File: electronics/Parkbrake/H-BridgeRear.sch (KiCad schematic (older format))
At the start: 82 parts

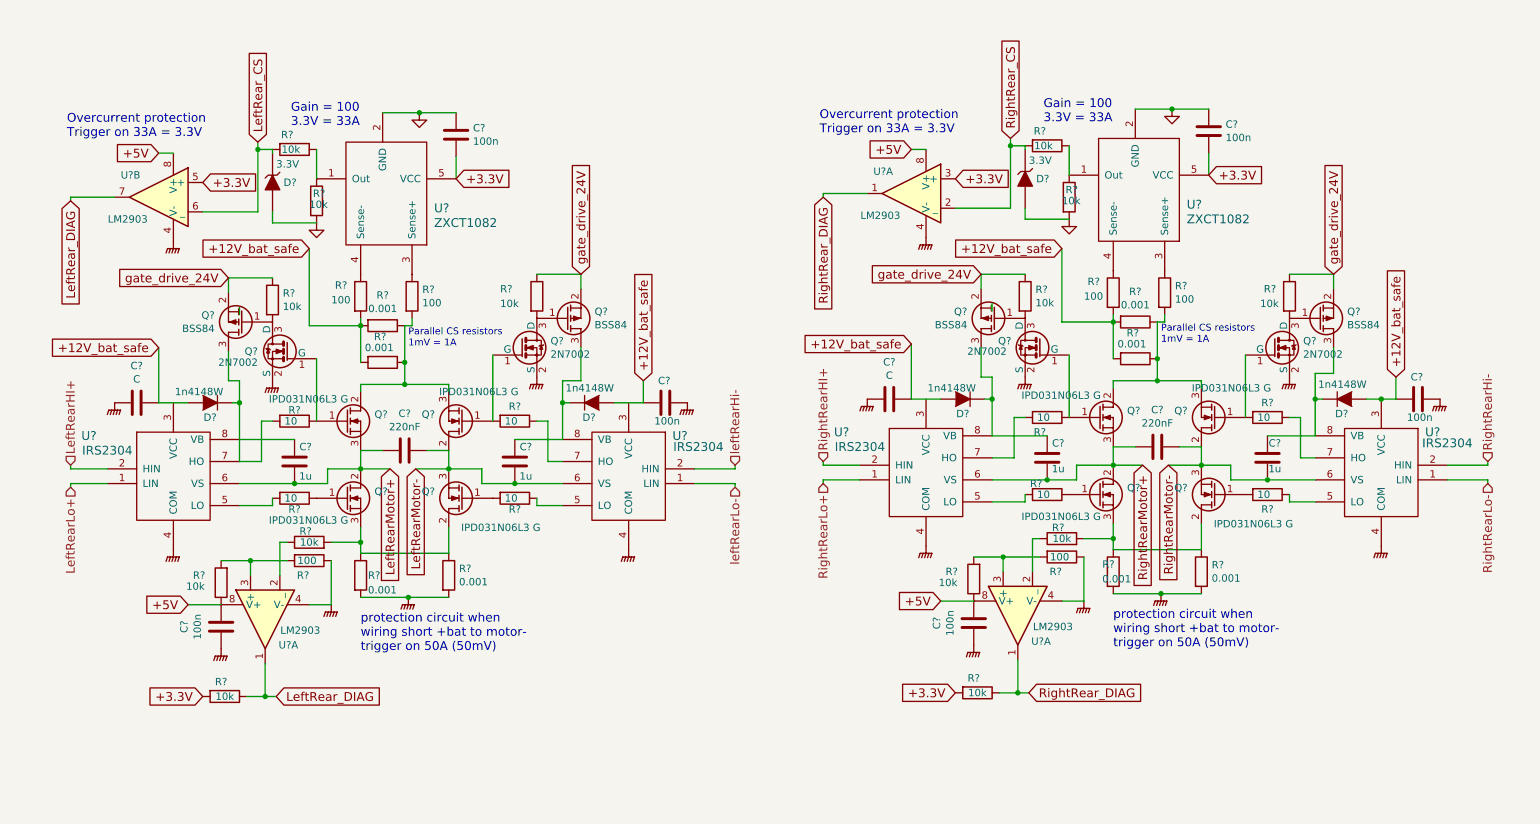
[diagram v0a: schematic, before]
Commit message: Fixes to Bat switch and polarity protection
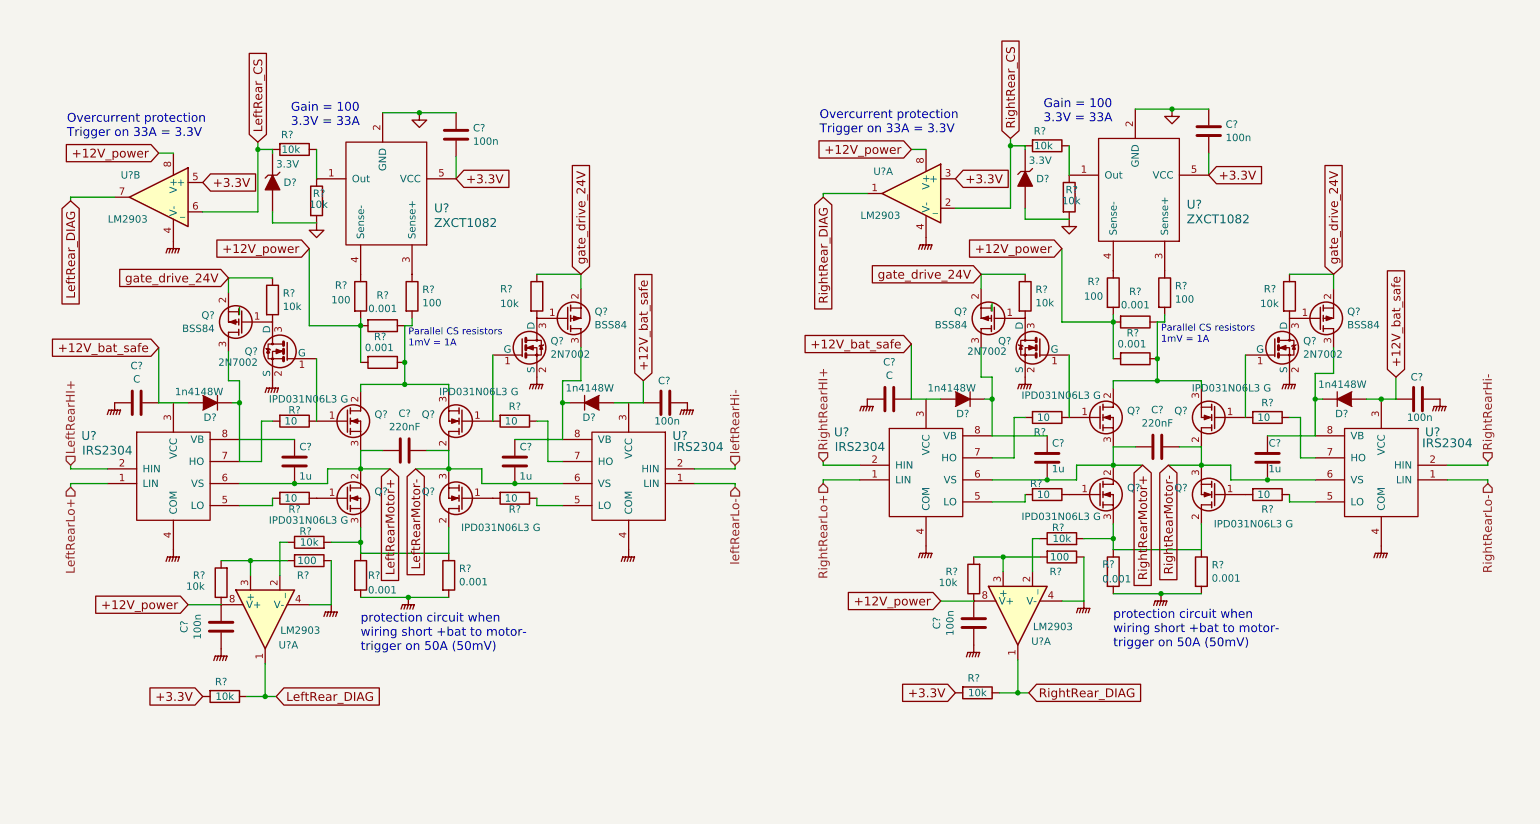
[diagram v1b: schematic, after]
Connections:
- net +12V_bat_safe: no longer R?.2, R?.2, R?.2, R?.2, R?.2, R?.2
- net +5V renamed +12V_power
- net +12V_power: now also R?.2, R?.2, R?.2, R?.2, R?.2, R?.2
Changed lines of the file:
@@
 $EndComp
 Text GLabel 2500 2475 0    60   Input ~ 0
-+12V_bat_safe
++12V_power
 $Comp
 L C C?
@@
 	2250 1800 2250 1825
 Text GLabel 1475 1825 0    60   Input ~ 0
-+5V
++12V_power
 Wire Wire Line
 	1575 1825 1475 1825
@@
 	875  2125 875  2150
 Text GLabel 1675 4900 0    60   Input ~ 0
-+5V
++12V_power
 Text GLabel 1775 2025 2    60   Input ~ 0
 +3.3V
@@
 $EndComp
 Text GLabel 7625 2475 0    60   Input ~ 0
-+12V_bat_safe
++12V_power
 $Comp
 L C C?
@@
 	7375 1775 7375 1800
 Text GLabel 6600 1800 0    60   Input ~ 0
-+5V
++12V_power
 Wire Wire Line
 	6700 1800 6600 1800
@@
 	6000 2100 6000 2125
 Text GLabel 6800 4875 0    60   Input ~ 0
-+5V
++12V_power
 Text GLabel 6900 2000 2    60   Input ~ 0
 +3.3V

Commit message: Add currentlimit latching to avaoid current limit oscilation Start a mcu schema part
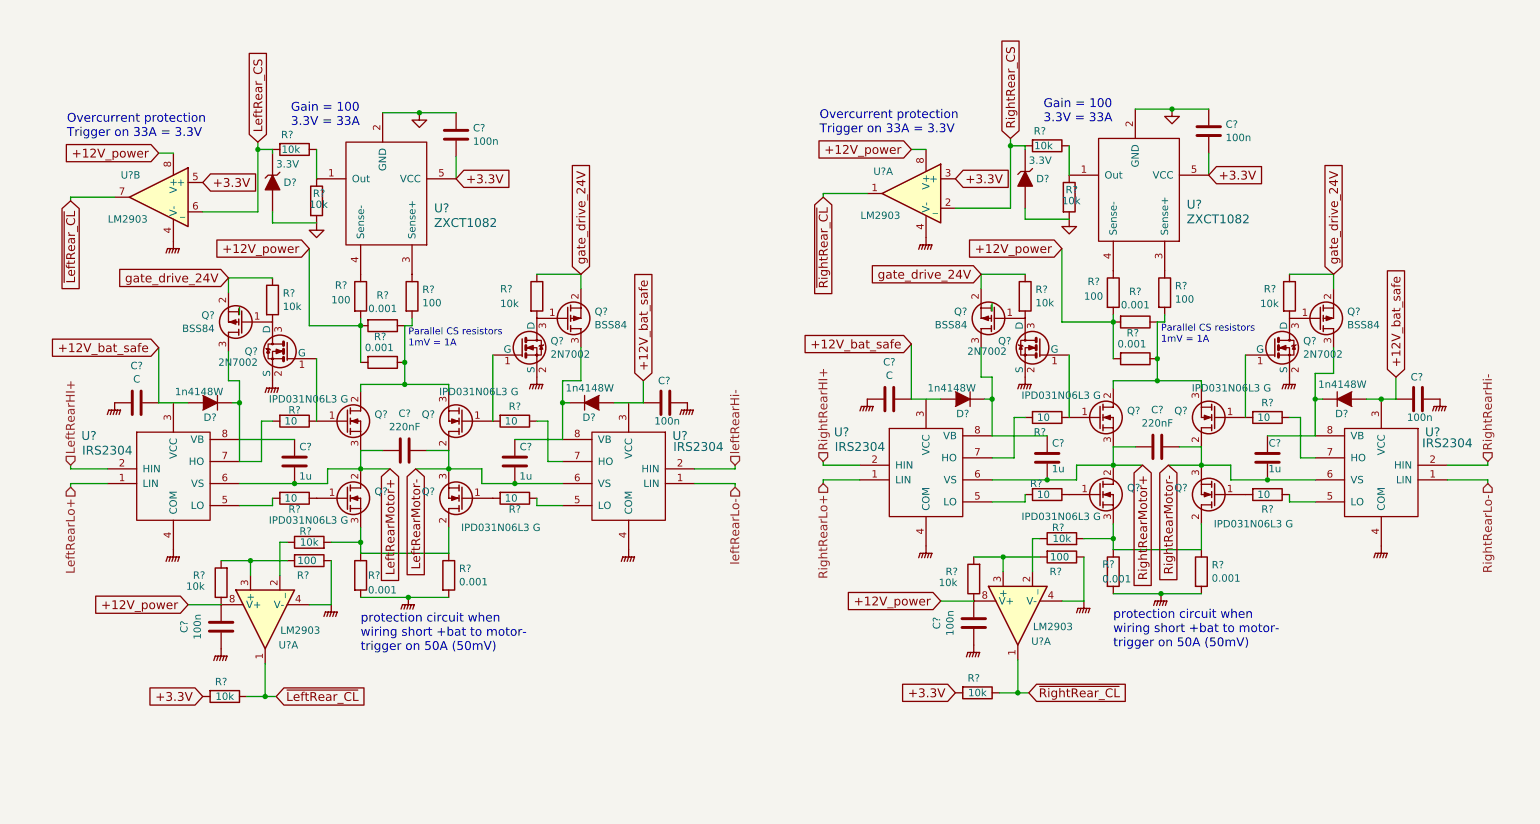
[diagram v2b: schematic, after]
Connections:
- net LeftRear_DIAG renamed ~LeftRear_CL
- net RightRear_DIAG renamed ~RightRear_CL
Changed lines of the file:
@@
 $Descr A4 11693 8268
 encoding utf-8
-Sheet 3 5
+Sheet 3 6
 Title ""
 Date ""
@@
 	4050 4225 4050 4175
 Text GLabel 2275 5525 2    60   Input ~ 0
-LeftRear_DIAG
+~LeftRear_CL
 Text GLabel 3050 3975 3    60   Input ~ 0
 LeftRearMotor+
@@
 LeftRear_CS
 Text GLabel 875  2150 3    60   Input ~ 0
-LeftRear_DIAG
+~LeftRear_CL
 Text GLabel 6000 2125 3    60   Input ~ 0
-RightRear_DIAG
+~RightRear_CL
 Text GLabel 7275 1725 1    60   Input ~ 0
 RightRear_CS
@@
 RightRearMotor-
 Text GLabel 7400 5500 2    60   Input ~ 0
-RightRear_DIAG
+~RightRear_CL
 $EndSCHEMATC

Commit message: More work on parkbrake node
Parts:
- R? (x4): footprint (none) -> Resistors_SMD:R_0805; farnell (none) -> 9332375; part (none) -> MC01W08051100R
- R? (x14): footprint (none) -> Resistors_SMD:R_0805; farnell (none) -> 9332391; part (none) -> MC01W0805110K
- R? (x8): footprint (none) -> Resistors_SMD:R_1206; farnell (none) -> 9335790; part (none) -> MC0125W1206110R
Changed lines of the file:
@@
 LIBS:teensy
 LIBS:power_switches
+LIBS:stm32
 LIBS:Parkbrake-cache
 EELAYER 25 0
@@
 $Descr A4 11693 8268
 encoding utf-8
-Sheet 3 6
+Sheet 3 10
 Title ""
 Date ""
@@
 F 0 "R?" H 3270 2846 50  0000 L CNN
 F 1 "100" H 3270 2755 50  0000 L CNN
-F 2 "" V 3130 2800 50  0000 C CNN
+F 2 "Resistors_SMD:R_0805" V 3130 2800 50  0001 C CNN
 F 3 "" H 3200 2800 50  0000 C CNN
+F 4 "MC01W08051100R" H 3200 2800 60  0001 C CNN "part"
+F 5 "9332375" H 3200 2800 60  0001 C CNN "farnell"
 	1    3200 2800
 	1    0    0    -1
@@
 F 0 "R?" H 2675 2875 50  0000 L CNN
 F 1 "100" H 2650 2775 50  0000 L CNN
-F 2 "" V 2780 2800 50  0000 C CNN
+F 2 "Resistors_SMD:R_0805" V 2780 2800 50  0001 C CNN
 F 3 "" H 2850 2800 50  0000 C CNN
+F 4 "MC01W08051100R" H 2850 2800 60  0001 C CNN "part"
+F 5 "9332375" H 2850 2800 60  0001 C CNN "farnell"
 	1    2850 2800
 	1    0    0    -1
@@
 F 0 "R?" H 2525 2200 50  0000 L CNN
 F 1 "10k" H 2500 2125 50  0000 L CNN
-F 2 "" V 2480 2150 50  0000 C CNN
+F 2 "Resistors_SMD:R_0805" V 2480 2150 50  0001 C CNN
 F 3 "" H 2550 2150 50  0000 C CNN
+F 4 "MC01W0805110K" H 2550 2150 60  0001 C CNN "part"
+F 5 "9332391" H 2550 2150 60  0001 C CNN "farnell"
 	1    2550 2150
 	1    0    0    -1
@@
 F 0 "R?" V 3975 4175 50  0000 C CNN
 F 1 "10" V 3900 4150 50  0000 C CNN
-F 2 "" V 3830 4175 50  0000 C CNN
+F 2 "Resistors_SMD:R_1206" V 3830 4175 50  0001 C CNN
 F 3 "" H 3900 4175 50  0000 C CNN
+F 4 "9335790" V 3900 4175 60  0001 C CNN "farnell"
+F 5 "MC0125W1206110R" V 3900 4175 60  0001 C CNN "part"
 	1    3900 4175
 	0    1    1    0
@@
 F 0 "R?" V 2475 4175 50  0000 C CNN
 F 1 "10" V 2400 4150 50  0000 C CNN
-F 2 "" V 2330 4175 50  0000 C CNN
+F 2 "Resistors_SMD:R_1206" V 2330 4175 50  0001 C CNN
 F 3 "" H 2400 4175 50  0000 C CNN
+F 4 "9335790" V 2400 4175 60  0001 C CNN "farnell"
+F 5 "MC0125W1206110R" V 2400 4175 60  0001 C CNN "part"
 	1    2400 4175
 	0    1    1    0
@@
 F 0 "R?" V 2325 3650 50  0000 C CNN
 F 1 "10" V 2400 3625 50  0000 C CNN
-F 2 "" V 2330 3650 50  0000 C CNN
+F 2 "Resistors_SMD:R_1206" V 2330 3650 50  0001 C CNN
 F 3 "" H 2400 3650 50  0000 C CNN
+F 4 "9335790" V 2400 3650 60  0001 C CNN "farnell"
+F 5 "MC0125W1206110R" V 2400 3650 60  0001 C CNN "part"
 	1    2400 3650
 	0    1    1    0
@@
 F 0 "R?" V 3800 3650 50  0000 C CNN
 F 1 "10" V 3900 3625 50  0000 C CNN
-F 2 "" V 3830 3650 50  0000 C CNN
+F 2 "Resistors_SMD:R_1206" V 3830 3650 50  0001 C CNN
 F 3 "" H 3900 3650 50  0000 C CNN
+F 4 "9335790" V 3900 3650 60  0001 C CNN "farnell"
+F 5 "MC0125W1206110R" V 3900 3650 60  0001 C CNN "part"
 	1    3900 3650
 	0    1    1    0
@@
 F 0 "R?" H 2050 4700 50  0000 C CNN
 F 1 "10k" H 2075 4775 50  0000 C CNN
-F 2 "" V 1830 4750 50  0000 C CNN
+F 2 "Resistors_SMD:R_0805" V 1830 4750 50  0001 C CNN
 F 3 "" H 1900 4750 50  0000 C CNN
+F 4 "MC01W0805110K" H 1900 4750 60  0001 C CNN "part"
+F 5 "9332391" H 1900 4750 60  0001 C CNN "farnell"
 	1    1900 4750
 	-1   0    0    1
@@
 F 0 "R?" V 2575 4500 50  0000 C CNN
 F 1 "10k" V 2500 4475 50  0000 C CNN
-F 2 "" V 2430 4475 50  0000 C CNN
+F 2 "Resistors_SMD:R_0805" V 2430 4475 50  0001 C CNN
 F 3 "" H 2500 4475 50  0000 C CNN
+F 4 "MC01W0805110K" V 2500 4475 60  0001 C CNN "part"
+F 5 "9332391" V 2500 4475 60  0001 C CNN "farnell"
 	1    2500 4475
 	0    -1   -1   0
@@
 F 0 "R?" V 1825 5500 50  0000 C CNN
 F 1 "10k" V 1925 5525 50  0000 C CNN
-F 2 "" V 1855 5525 50  0000 C CNN
+F 2 "Resistors_SMD:R_0805" V 1855 5525 50  0001 C CNN
 F 3 "" H 1925 5525 50  0000 C CNN
+F 4 "MC01W0805110K" V 1925 5525 60  0001 C CNN "part"
+F 5 "9332391" V 1925 5525 60  0001 C CNN "farnell"
 	1    1925 5525
 	0    1    1    0
@@
 F 0 "R?" V 2300 1750 50  0000 C CNN
 F 1 "10k" V 2400 1775 50  0000 C CNN
-F 2 "" V 2330 1800 50  0000 C CNN
+F 2 "Resistors_SMD:R_0805" V 2330 1800 50  0001 C CNN
 F 3 "" H 2400 1800 50  0000 C CNN
+F 4 "MC01W0805110K" V 2400 1800 60  0001 C CNN "part"
+F 5 "9332391" V 2400 1800 60  0001 C CNN "farnell"
 	1    2400 1800
 	0    1    1    0
@@
 F 0 "R?" H 8395 2821 50  0000 L CNN
 F 1 "100" H 8395 2730 50  0000 L CNN
-F 2 "" V 8255 2775 50  0000 C CNN
+F 2 "Resistors_SMD:R_0805" V 8255 2775 50  0001 C CNN
 F 3 "" H 8325 2775 50  0000 C CNN
+F 4 "MC01W08051100R" H 8325 2775 60  0001 C CNN "part"
+F 5 "9332375" H 8325 2775 60  0001 C CNN "farnell"
 	1    8325 2775
 	1    0    0    -1
@@
 F 0 "R?" H 7800 2850 50  0000 L CNN
 F 1 "100" H 7775 2750 50  0000 L CNN
-F 2 "" V 7905 2775 50  0000 C CNN
+F 2 "Resistors_SMD:R_0805" V 7905 2775 50  0001 C CNN
 F 3 "" H 7975 2775 50  0000 C CNN
+F 4 "MC01W08051100R" H 7975 2775 60  0001 C CNN "part"
+F 5 "9332375" H 7975 2775 60  0001 C CNN "farnell"
 	1    7975 2775
 	1    0    0    -1
@@
 F 0 "R?" H 7650 2175 50  0000 L CNN
 F 1 "10k" H 7625 2100 50  0000 L CNN
-F 2 "" V 7605 2125 50  0000 C CNN
+F 2 "Resistors_SMD:R_0805" V 7605 2125 50  0001 C CNN
 F 3 "" H 7675 2125 50  0000 C CNN
+F 4 "MC01W0805110K" H 7675 2125 60  0001 C CNN "part"
+F 5 "9332391" H 7675 2125 60  0001 C CNN "farnell"
 	1    7675 2125
 	1    0    0    -1
@@
 F 0 "R?" V 9125 4150 50  0000 C CNN
 F 1 "10" V 9025 4125 50  0000 C CNN
-F 2 "" V 8955 4150 50  0000 C CNN
+F 2 "Resistors_SMD:R_1206" V 8955 4150 50  0001 C CNN
 F 3 "" H 9025 4150 50  0000 C CNN
+F 4 "9335790" V 9025 4150 60  0001 C CNN "farnell"
+F 5 "MC0125W1206110R" V 9025 4150 60  0001 C CNN "part"
 	1    9025 4150
 	0    1    1    0
@@
 F 0 "R?" V 7450 4075 50  0000 C CNN
 F 1 "10" V 7525 4125 50  0000 C CNN
-F 2 "" V 7455 4150 50  0000 C CNN
+F 2 "Resistors_SMD:R_1206" V 7455 4150 50  0001 C CNN
 F 3 "" H 7525 4150 50  0000 C CNN
+F 4 "9335790" V 7525 4150 60  0001 C CNN "farnell"
+F 5 "MC0125W1206110R" V 7525 4150 60  0001 C CNN "part"
 	1    7525 4150
 	0    1    1    0
@@
 F 0 "R?" V 7625 3575 50  0000 C CNN
 F 1 "10" V 7525 3600 50  0000 C CNN
-F 2 "" V 7455 3625 50  0000 C CNN
+F 2 "Resistors_SMD:R_1206" V 7455 3625 50  0001 C CNN
 F 3 "" H 7525 3625 50  0000 C CNN
+F 4 "9335790" V 7525 3625 60  0001 C CNN "farnell"
+F 5 "MC0125W1206110R" V 7525 3625 60  0001 C CNN "part"
 	1    7525 3625
 	0    1    1    0
@@
 F 0 "R?" V 8925 3625 50  0000 C CNN
 F 1 "10" V 9025 3600 50  0000 C CNN
-F 2 "" V 8955 3625 50  0000 C CNN
+F 2 "Resistors_SMD:R_1206" V 8955 3625 50  0001 C CNN
 F 3 "" H 9025 3625 50  0000 C CNN
+F 4 "9335790" V 9025 3625 60  0001 C CNN "farnell"
+F 5 "MC0125W1206110R" V 9025 3625 60  0001 C CNN "part"
 	1    9025 3625
 	0    1    1    0
@@
 F 0 "R?" H 7175 4675 50  0000 C CNN
 F 1 "10k" H 7200 4750 50  0000 C CNN
-F 2 "" V 6955 4725 50  0000 C CNN
+F 2 "Resistors_SMD:R_0805" V 6955 4725 50  0001 C CNN
 F 3 "" H 7025 4725 50  0000 C CNN
+F 4 "MC01W0805110K" H 7025 4725 60  0001 C CNN "part"
+F 5 "9332391" H 7025 4725 60  0001 C CNN "farnell"
 	1    7025 4725
 	-1   0    0    1
@@
 F 0 "R?" V 7700 4475 50  0000 C CNN
 F 1 "10k" V 7625 4450 50  0000 C CNN
-F 2 "" V 7555 4450 50  0000 C CNN
+F 2 "Resistors_SMD:R_0805" V 7555 4450 50  0001 C CNN
 F 3 "" H 7625 4450 50  0000 C CNN
+F 4 "MC01W0805110K" V 7625 4450 60  0001 C CNN "part"
+F 5 "9332391" V 7625 4450 60  0001 C CNN "farnell"
 	1    7625 4450
 	0    -1   -1   0
@@
 F 0 "R?" V 6950 5475 50  0000 C CNN
 F 1 "10k" V 7050 5500 50  0000 C CNN
-F 2 "" V 6980 5500 50  0000 C CNN
+F 2 "Resistors_SMD:R_0805" V 6980 5500 50  0001 C CNN
 F 3 "" H 7050 5500 50  0000 C CNN
+F 4 "MC01W0805110K" V 7050 5500 60  0001 C CNN "part"
+F 5 "9332391" V 7050 5500 60  0001 C CNN "farnell"
 	1    7050 5500
 	0    1    1    0
@@
 F 0 "R?" V 7425 1725 50  0000 C CNN
 F 1 "10k" V 7525 1750 50  0000 C CNN
-F 2 "" V 7455 1775 50  0000 C CNN
+F 2 "Resistors_SMD:R_0805" V 7455 1775 50  0001 C CNN
 F 3 "" H 7525 1775 50  0000 C CNN
+F 4 "MC01W0805110K" V 7525 1775 60  0001 C CNN "part"
+F 5 "9332391" V 7525 1775 60  0001 C CNN "farnell"
 	1    7525 1775
 	0    1    1    0
@@
 F 0 "R?" H 3800 2850 50  0000 L CNN
 F 1 "10k" H 3800 2750 50  0000 L CNN
-F 2 "" V 3980 2800 50  0000 C CNN
+F 2 "Resistors_SMD:R_0805" V 3980 2800 50  0001 C CNN
 F 3 "" H 4050 2800 50  0000 C CNN
+F 4 "MC01W0805110K" H 4050 2800 60  0001 C CNN "part"
+F 5 "9332391" H 4050 2800 60  0001 C CNN "farnell"
 	1    4050 2800
 	1    0    0    -1
@@
 F 0 "R?" H 2320 2871 50  0000 L CNN
 F 1 "10k" H 2320 2780 50  0000 L CNN
-F 2 "" V 2180 2825 50  0000 C CNN
+F 2 "Resistors_SMD:R_0805" V 2180 2825 50  0001 C CNN
 F 3 "" H 2250 2825 50  0000 C CNN
+F 4 "MC01W0805110K" H 2250 2825 60  0001 C CNN "part"
+F 5 "9332391" H 2250 2825 60  0001 C CNN "farnell"
 	1    2250 2825
 	1    0    0    -1
@@
 F 0 "R?" H 9000 2850 50  0000 L CNN
 F 1 "10k" H 8975 2750 50  0000 L CNN
-F 2 "" V 9105 2800 50  0000 C CNN
+F 2 "Resistors_SMD:R_0805" V 9105 2800 50  0001 C CNN
 F 3 "" H 9175 2800 50  0000 C CNN
+F 4 "MC01W0805110K" H 9175 2800 60  0001 C CNN "part"
+F 5 "9332391" H 9175 2800 60  0001 C CNN "farnell"
 	1    9175 2800
 	1    0    0    -1
@@
 F 0 "R?" H 7445 2846 50  0000 L CNN
 F 1 "10k" H 7445 2755 50  0000 L CNN
-F 2 "" V 7305 2800 50  0000 C CNN
+F 2 "Resistors_SMD:R_0805" V 7305 2800 50  0001 C CNN
 F 3 "" H 7375 2800 50  0000 C CNN
+F 4 "MC01W0805110K" H 7375 2800 60  0001 C CNN "part"
+F 5 "9332391" H 7375 2800 60  0001 C CNN "farnell"
 	1    7375 2800
 	1    0    0    -1
